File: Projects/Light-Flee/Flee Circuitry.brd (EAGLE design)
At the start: 68.6 x 53.3 mm, 8 parts

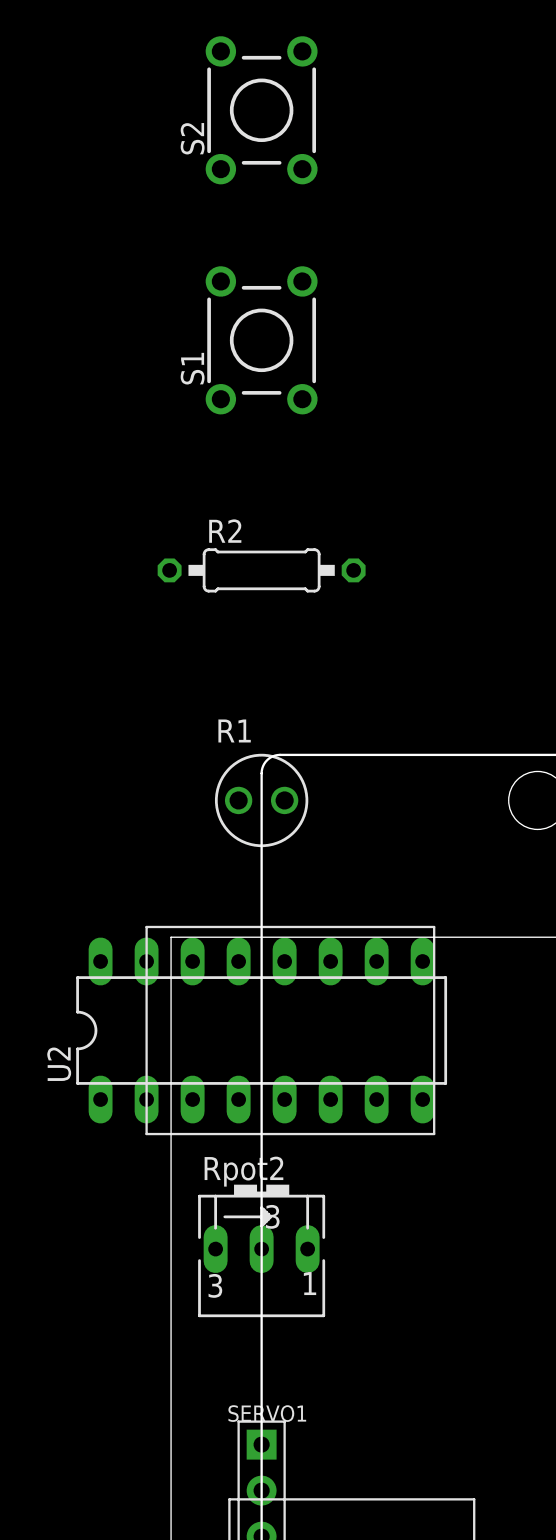
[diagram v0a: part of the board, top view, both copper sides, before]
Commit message: refactored repository to have a project based approach with specialized code and circuitry for each project with the rover
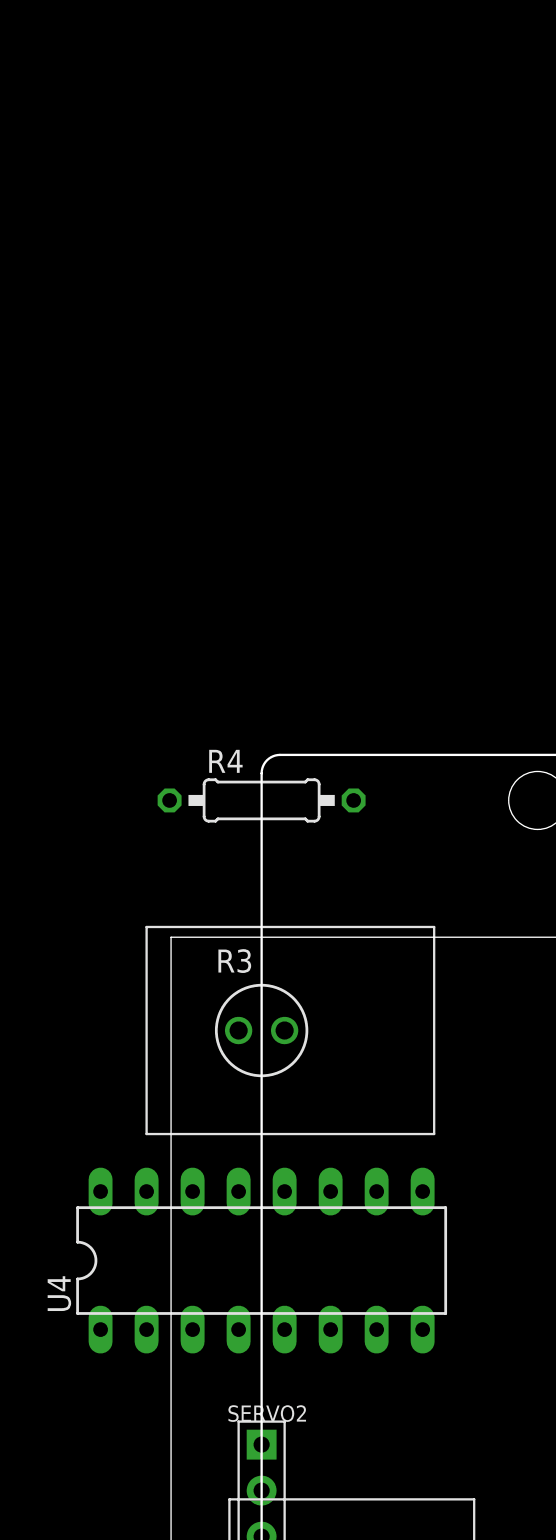
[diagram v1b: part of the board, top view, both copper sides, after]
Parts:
- ULight Control: renamed from U3
- removed R1: (no value), AUTODESK_CIRCUITS_BREADBOARD:PHOTORESISTOR-2.54
- removed R2: 1k‎Ω, AUTODESK_CIRCUITS_BREADBOARD:0207/10
- removed Rpot2: 250k‎Ω, AUTODESK_CIRCUITS_BREADBOARD:B25V
- removed S1, S2: (no value), AUTODESK_CIRCUITS_BREADBOARD:TL1105
- removed U2: (no value), AUTODESK_CIRCUITS_BREADBOARD:DIL16
- added R3: (no value), AUTODESK_CIRCUITS_BREADBOARD:PHOTORESISTOR-2.54
- added R4: 10000‎Ω, AUTODESK_CIRCUITS_BREADBOARD:0207/10
- added U4: (no value), AUTODESK_CIRCUITS_BREADBOARD:DIL16
- renumbered SERVO1 to SERVO2
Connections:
- removed net N$1 (its old number): U2.1
- removed net N$18: S1.3, ULight Control.A4
- removed net N$19: S2.2
- removed net N$20: S2.3, ULight Control.A3
- removed net N$21: Rpot2.E
- removed net N$22: Rpot2.A
- removed net N$23: Rpot2.S
- new net N$13: U4.14
- net N$10: now also U4.11; no longer U2.14
- net N$11: now also U4.12; no longer U2.15
- net N$12: now also U4.13; no longer R1.P$2, S1.1, S2.1, SERVO2.2, U2.16, U2.9, ULight Control.5V
- net N$14: now also U4.15; no longer U2.8
- net N$15: now also U4.16; no longer U2.5
- net N$16: now also R3.P$2, R4.1; no longer R1.P$1, R2.1
- net N$17: now also R4.2, SERVO2.1, U4.4, U4.5, ULight Control.GND..; no longer S1.2
- net N$2: now also U4.1, ULight Control.13; no longer U2.4
- net N$3: now also U4.2, ULight Control.11; no longer U2.2
- net N$4: now also U4.3; no longer U2.3
- net N$5: now also U4.6; no longer U2.6
- net N$6: now also U4.7, ULight Control.9; no longer U2.7
- net N$7: now also R3.P$1, SERVO2.2, U4.8, ULight Control.5V; no longer U2.10
- net N$8: now also U4.9; no longer U2.11
- net N$9: now also U4.10; no longer R2.2, S1.4, S2.4, SERVO2.1, U2.12, U2.13, ULight Control.GND..
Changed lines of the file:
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@@
 </autorouter>
 <elements>
-<element value="" name="U3" library="AUTODESK_CIRCUITS_BREADBOARD" package="ARDUINO_UNO" x="5" y="10.08"></element><element value="" name="SERVO1" library="AUTODESK_CIRCUITS_BREADBOARD" package="1X3P-2.54-2.54-11.6-3.0-BLACK-MALE" x="5" y="22.78"></element><element value="250k‎Ω" name="Rpot2" library="AUTODESK_CIRCUITS_BREADBOARD" package="B25V" x="5" y="35.480000000000004"></element><element value="" name="U2" library="AUTODESK_CIRCUITS_BREADBOARD" package="DIL16" x="5" y="48.18"></element><element value="" name="R1" library="AUTODESK_CIRCUITS_BREADBOARD" package="PHOTORESISTOR-2.54" x="5" y="60.879999999999995"></element><element value="1k‎Ω" name="R2" library="AUTODESK_CIRCUITS_BREADBOARD" package="0207/10" x="5" y="73.58"></element><element value="" name="S1" library="AUTODESK_CIRCUITS_BREADBOARD" package="TL1105" x="5" y="86.28"></element><element value="" name="S2" library="AUTODESK_CIRCUITS_BREADBOARD" package="TL1105" x="5" y="98.98"></element></elements>
+<element value="" name="ULight Control" library="AUTODESK_CIRCUITS_BREADBOARD" package="ARDUINO_UNO" x="5" y="10.08"></element><element value="" name="SERVO2" library="AUTODESK_CIRCUITS_BREADBOARD" package="1X3P-2.54-2.54-11.6-3.0-BLACK-MALE" x="5" y="22.78"></element><element value="" name="U4" library="AUTODESK_CIRCUITS_BREADBOARD" package="DIL16" x="5" y="35.480000000000004"></element><element value="" name="R3" library="AUTODESK_CIRCUITS_BREADBOARD" package="PHOTORESISTOR-2.54" x="5" y="48.18"></element><element value="10000‎Ω" name="R4" library="AUTODESK_CIRCUITS_BREADBOARD" package="0207/10" x="5" y="60.879999999999995"></element></elements>
 <signals>
-<signal name="N$1"><contactref element="U2" pad="1"></contactref></signal><signal name="N$2"><contactref element="U2" pad="4"></contactref></signal><signal name="N$3"><contactref element="U2" pad="2"></contactref></signal><signal name="N$4"><contactref element="U2" pad="3"></contactref></signal><signal name="N$5"><contactref element="U2" pad="6"></contactref></signal><signal name="N$6"><contactref element="U2" pad="7"></contactref></signal><signal name="N$7"><contactref element="U2" pad="10"></contactref></signal><signal name="N$8"><contactref element="U2" pad="11"></contactref></signal><signal name="N$9"><contactref element="U2" pad="12"></contactref><contactref element="U2" pad="13"></contactref><wire x1="6.27" y1="51.99" x2="3.73" y2="51.99" width="0" layer="19" extent="1-1"></wire><contactref element="U3" pad="GND.."></contactref><wire x1="3.73" y1="51.99" x2="45.64" y2="12.620000000000001" width="0" layer="19" extent="1-1"></wire><contactref element="SERVO1" pad="1"></contactref><wire x1="45.64" y1="12.620000000000001" x2="5" y2="25.32" width="0" layer="19" extent="1-1"></wire><contactref element="R2" pad="2"></contactref><wire x1="5" y1="25.32" x2="10.08" y2="73.58" width="0" layer="19" extent="1-1"></wire><contactref element="S1" pad="4"></contactref><wire x1="10.08" y1="73.58" x2="7.25" y2="83.03" width="0" layer="19" extent="1-1"></wire><contactref element="S2" pad="4"></contactref><wire x1="7.25" y1="83.03" x2="7.25" y2="95.73" width="0" layer="19" extent="1-1"></wire></signal><signal name="N$10"><contactref element="U2" pad="14"></contactref></signal><signal name="N$11"><contactref element="U2" pad="15"></contactref></signal><signal name="N$12"><contactref element="U2" pad="16"></contactref><contactref element="U2" pad="9"></contactref><wire x1="-3.8900000000000006" y1="51.99" x2="13.89" y2="51.99" width="0" layer="19" extent="1-1"></wire><contactref element="U3" pad="5V"></contactref><wire x1="13.89" y1="51.99" x2="43.1" y2="12.620000000000001" width="0" layer="19" extent="1-1"></wire><contactref element="SERVO1" pad="2"></contactref><wire x1="43.1" y1="12.620000000000001" x2="5" y2="22.78" width="0" layer="19" extent="1-1"></wire><contactref element="R1" pad="P$2"></contactref><wire x1="5" y1="22.78" x2="6.27" y2="60.879999999999995" width="0" layer="19" extent="1-1"></wire><contactref element="S1" pad="1"></contactref><wire x1="6.27" y1="60.879999999999995" x2="2.75" y2="89.53" width="0" layer="19" extent="1-1"></wire><contactref element="S2" pad="1"></contactref><wire x1="2.75" y1="89.53" x2="2.75" y2="102.23" width="0" layer="19" extent="1-1"></wire></signal><signal name="N$13"><contactref element="U3" pad="3"></contactref><contactref element="SERVO1" pad="3"></contactref><wire x1="60.88" y1="60.879999999999995" x2="5" y2="20.240000000000002" width="0" layer="19" extent="1-1"></wire></signal><signal name="N$14"><contactref element="U2" pad="8"></contactref></signal><signal name="N$15"><contactref element="U2" pad="5"></contactref></signal><signal name="N$16"><contactref element="R1" pad="P$1"></contactref><contactref element="U3" pad="A0"></contactref><wire x1="3.73" y1="60.879999999999995" x2="55.8" y2="12.620000000000001" width="0" layer="19" extent="1-1"></wire><contactref element="R2" pad="1"></contactref><wire x1="55.8" y1="12.620000000000001" x2="-0.08000000000000007" y2="73.58" width="0" layer="19" extent="1-1"></wire></signal><signal name="N$17"><contactref element="S1" pad="2"></contactref></signal><signal name="N$18"><contactref element="S1" pad="3"></contactref><contactref element="U3" pad="A4"></contactref><wire x1="2.75" y1="83.03" x2="65.96000000000001" y2="12.620000000000001" width="0" layer="19" extent="1-1"></wire></signal><signal name="N$19"><contactref element="S2" pad="2"></contactref></signal><signal name="N$20"><contactref element="S2" pad="3"></contactref><contactref element="U3" pad="A3"></contactref><wire x1="2.75" y1="95.73" x2="63.42" y2="12.620000000000001" width="0" layer="19" extent="1-1"></wire></signal><signal name="N$21"><contactref element="Rpot2" pad="E"></contactref></signal><signal name="N$22"><contactref element="Rpot2" pad="A"></contactref></signal><signal name="N$23"><contactref element="Rpot2" pad="S"></contactref></signal></signals>
+<signal name="N$1"><contactref element="SERVO2" pad="3"></contactref><contactref element="ULight Control" pad="3"></contactref><wire x1="5" y1="20.240000000000002" x2="60.88" y2="60.879999999999995" width="0" layer="19" extent="1-1"></wire></signal><signal name="N$2"><contactref element="U4" pad="1"></contactref><contactref element="ULight Control" pad="13"></contactref><wire x1="-3.8900000000000006" y1="31.670000000000005" x2="33.956" y2="60.879999999999995" width="0" layer="19" extent="1-1"></wire></signal><signal name="N$3"><contactref element="U4" pad="2"></contactref><contactref element="ULight Control" pad="11"></contactref><wire x1="-1.3499999999999996" y1="31.670000000000005" x2="39.036" y2="60.879999999999995" width="0" layer="19" extent="1-1"></wire></signal><signal name="N$4"><contactref element="U4" pad="3"></contactref></signal><signal name="N$5"><contactref element="U4" pad="6"></contactref></signal><signal name="N$6"><contactref element="U4" pad="7"></contactref><contactref element="ULight Control" pad="9"></contactref><wire x1="11.35" y1="31.670000000000005" x2="44.116" y2="60.879999999999995" width="0" layer="19" extent="1-1"></wire></signal><signal name="N$7"><contactref element="U4" pad="8"></contactref><contactref element="SERVO2" pad="2"></contactref><wire x1="13.89" y1="31.670000000000005" x2="5" y2="22.78" width="0" layer="19" extent="1-1"></wire><contactref element="ULight Control" pad="5V"></contactref><wire x1="5" y1="22.78" x2="43.1" y2="12.620000000000001" width="0" layer="19" extent="1-1"></wire><contactref element="R3" pad="P$1"></contactref><wire x1="43.1" y1="12.620000000000001" x2="3.73" y2="48.18" width="0" layer="19" extent="1-1"></wire></signal><signal name="N$8"><contactref element="U4" pad="9"></contactref></signal><signal name="N$9"><contactref element="U4" pad="10"></contactref></signal><signal name="N$10"><contactref element="U4" pad="11"></contactref></signal><signal name="N$11"><contactref element="U4" pad="12"></contactref></signal><signal name="N$12"><contactref element="U4" pad="13"></contactref></signal><signal name="N$13"><contactref element="U4" pad="14"></contactref></signal><signal name="N$14"><contactref element="U4" pad="15"></contactref></signal><signal name="N$15"><contactref element="U4" pad="16"></contactref></signal><signal name="N$16"><contactref element="R3" pad="P$2"></contactref><contactref element="ULight Control" pad="A0"></contactref><wire x1="6.27" y1="48.18" x2="55.8" y2="12.620000000000001" width="0" layer="19" extent="1-1"></wire><contactref element="R4" pad="1"></contactref><wire x1="55.8" y1="12.620000000000001" x2="-0.08000000000000007" y2="60.879999999999995" width="0" layer="19" extent="1-1"></wire></signal><signal name="N$17"><contactref element="R4" pad="2"></contactref><contactref element="U4" pad="4"></contactref><wire x1="10.08" y1="60.879999999999995" x2="3.73" y2="31.670000000000005" width="0" layer="19" extent="1-1"></wire><contactref element="U4" pad="5"></contactref><wire x1="3.73" y1="31.670000000000005" x2="6.27" y2="31.670000000000005" width="0" layer="19" extent="1-1"></wire><contactref element="SERVO2" pad="1"></contactref><wire x1="6.27" y1="31.670000000000005" x2="5" y2="25.32" width="0" layer="19" extent="1-1"></wire><contactref element="ULight Control" pad="GND.."></contactref><wire x1="5" y1="25.32" x2="45.64" y2="12.620000000000001" width="0" layer="19" extent="1-1"></wire></signal></signals>
 </board>
 </drawing>
